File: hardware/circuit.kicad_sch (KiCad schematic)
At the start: 66 parts, among them J1 VBUS input fly-leads, J2 Shunt Kelvin, J3 Piezo fly-lead, J4 ESC1 signal, J5 ESC2 signal, J6 ELRS receiver, U1 Seeed XIAO RP2350, U10 SK9822-EC20, U2 AP63205WU-7, U3 MCP23S17T-E/SS, U4 H3LIS331DLTR, U5 H3LIS331DLTR, U6 H3LIS331DLTR, U7 INA180A1IDBVR, U8 SN74AHCT1G125, U9 SN74AHCT1G125

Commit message: feat: almost full schematic
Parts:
- removed C1, C4, C5: 22uF, Capacitor_SMD:C_0805_2012Metric, symbol Device:C_Small
- removed C12, C2, C3: 100nF, Capacitor_SMD:C_0402_1005Metric, symbol Device:C_Small
- removed C6: 10uF, Capacitor_SMD:C_0603_1608Metric, symbol Device:C_Small
- removed D1: BAT54S, Package_TO_SOT_SMD:SOT-23, symbol Diode:BAT54S
- removed J1: VBUS input fly-leads, Connector_Wire:SolderWire-0.5sqmm_1x02_P4.6mm_D0.9mm_OD2.1mm_Relief, symbol Connector_Generic:Conn_01x02
- removed J5: ESC2 signal, Connector_Wire:SolderWire-0.25sqmm_1x02_P4.2mm_D0.65mm_OD1.7mm_Relief, symbol Connector_Generic:Conn_01x02
- removed J6: ELRS receiver, Connector_Wire:SolderWire-0.25sqmm_1x04_P4.2mm_D0.65mm_OD1.7mm_Relief, symbol Connector_Generic:Conn_01x04
- removed L1: 4.7uH, Inductor_SMD:L_Wuerth_MAPI-4020, symbol Device:L_Small
- removed R10: 33kΩ, Resistor_SMD:R_0402_1005Metric, symbol Device:R_Small
- removed R9: 100kΩ, Resistor_SMD:R_0402_1005Metric, symbol Device:R_Small
- removed TP1: TP_SCK, TestPoint:TestPoint_Pad_D1.0mm, symbol Connector:TestPoint
- removed TP10: TP_VBAT, TestPoint:TestPoint_Pad_D1.0mm, symbol Connector:TestPoint
- removed TP12: TP_PIEZO, TestPoint:TestPoint_Pad_D1.0mm, symbol Connector:TestPoint
- removed TP16: TP_3V3, TestPoint:TestPoint_Pad_D1.0mm, symbol Connector:TestPoint
- removed TP17: TP_5V, TestPoint:TestPoint_Pad_D1.0mm, symbol Connector:TestPoint
- removed TP2: TP_CS_A, TestPoint:TestPoint_Pad_D1.0mm, symbol Connector:TestPoint
- removed TP3: TP_CS_B, TestPoint:TestPoint_Pad_D1.0mm, symbol Connector:TestPoint
- removed TP4: TP_CS_C, TestPoint:TestPoint_Pad_D1.0mm, symbol Connector:TestPoint
- removed TP5: TP_MISO, TestPoint:TestPoint_Pad_D1.0mm, symbol Connector:TestPoint
- removed TP6: TP_DS1, TestPoint:TestPoint_Pad_D1.0mm, symbol Connector:TestPoint
- removed TP7: TP_DS2, TestPoint:TestPoint_Pad_D1.0mm, symbol Connector:TestPoint
- removed TP8: TP_CRSF_RX, TestPoint:TestPoint_Pad_D1.0mm, symbol Connector:TestPoint
- removed TP9: TP_CRSF_TX, TestPoint:TestPoint_Pad_D1.0mm, symbol Connector:TestPoint
- removed U2: AP63205WU-7, Library:TSOT-23-6_L2.9-W1.6-P0.95-LS2.8-BL, symbol Library:AP63205WU-7
- removed U7: INA180A1IDBVR, Library:SOT-23-5_L3.0-W1.7-P0.95-LS2.8-BR, symbol Library:INA180A1IDBVR
- added C17, C21, C22: 22uF, Capacitor_SMD:C_0805_2012Metric, symbol Device:C_Small
- added C18, C20: 100nF, Capacitor_SMD:C_0402_1005Metric, symbol Device:C_Small
- added C19: 10uF, Capacitor_SMD:C_0603_1608Metric, symbol Device:C_Small
- added D3, D4: PESD5V0V1BB, Diode_SMD:D_SOD-523, symbol Device:D_TVS
- added D5: SMAJ12CA, Diode_SMD:D_SMA, symbol Device:D_TVS
- added L2: 4.7uH, Inductor_SMD:L_Wuerth_MAPI-4020, symbol Device:L_Small
- added Q1: AO3402, Library:SOT-23_L2.9-W1.3-P1.90-LS2.4-BR, symbol Library:AO3402_C14385
- added R16: 100Ω, Resistor_SMD:R_0402_1005Metric, symbol Device:R_Small
- added R17: 100kΩ, Resistor_SMD:R_0402_1005Metric, symbol Device:R_Small
- added R18: 33kΩ, Resistor_SMD:R_0402_1005Metric, symbol Device:R_Small
- added TP18: TP_3V3, TestPoint:TestPoint_Pad_D1.0mm, symbol Connector:TestPoint
- added TP19: TP_5V, TestPoint:TestPoint_Pad_D1.0mm, symbol Connector:TestPoint
- added U11: AP63205WU-7, Library:TSOT-23-6_L2.9-W1.6-P0.95-LS2.8-BL, symbol Library:AP63205WU-7
- added U7: BetaFPV ELRS Lite, Library:BetaFPV_ELRS_Lite, symbol Connector_Generic:Conn_01x04
- C13: value 10nF -> 100nF
- J2: value Shunt Kelvin -> Orange TinySLED
- J3: value Piezo fly-lead -> VBUS input fly-leads; footprint Connector_Wire:SolderWire-0.25sqmm_1x02_P4.2mm_D0.65mm_OD1.7mm_Relief -> Connector_Wire:SolderWire-0.5sqmm_1x02_P4.6mm_D0.9mm_OD2.1mm_Relief
- J4: value ESC1 signal -> AM32 dual ESC; footprint Connector_Wire:SolderWire-0.25sqmm_1x02_P4.2mm_D0.65mm_OD1.7mm_Relief -> Connector_Wire:SolderWire-0.25sqmm_1x04_P4.2mm_D0.65mm_OD1.7mm_Relief; symbol Connector_Generic:Conn_01x02 -> Connector_Generic:Conn_01x04
- R11: value 1MΩ -> 100kΩ
- TP11: value TP_CURR -> TP_VBAT
- U4: value H3LIS331DLTR -> LSM6DSV320XTR; footprint Library:LGA-16_L3.0-W3.0-P0.50-BL -> Library:LGA-14_L3.0-W2.5-P0.50-TL; symbol Library:H3LIS331DLTR -> Library:LSM6DSV320XTR; LCSC Part C2655074 -> C26633007
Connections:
- net 3V3: now also U4.5 (VDDIO), U4.8 (VDD), C19.1, TP18.1; no longer U4.1 (Vdd_IO), U4.14 (Vdd), U4.15 (Reserved)
- net 5V: now also C21.1, C22.1, L2.2, TP19.1, U11.1 (FB), U7.3 (Pin_3)
- net CRSF_RX: now also U7.2 (Pin_2)
- net CRSF_TX: now also U7.1 (Pin_1)
- net CS_A: now also U4.12 (CS); no longer U4.8 (CS)
- net GND: now also J4.1 (Pin_1), J4.4 (Pin_4), U4.2 (SDx), U4.3 (SCx), U4.6 (GND), U4.7 (GND), C17.2, C18.2, C19.2, C21.2, C22.2, D3.2 (A2), D4.2 (A2), D5.2 (A2), Q1.2 (S), R17.2, R18.2, U11.4 (GND), U7.4 (Pin_4); no longer J4.2 (Pin_2), R11.2, U4.10 (Reserved), U4.12 (GND), U4.13 (GND), U4.16 (GND), U4.5 (GND)
- net LED_OE_N: now also U1.3 (D2/A2/GPIO42); no longer U3.24 (GPA3)
- net MISO_A: now also U4.1 (SDO/TA0); no longer U4.7 (SDO/SA0)
- net SPI_MOSI: now also U4.14 (SDA); no longer U4.6 (SDA/SDI/SDO)
- net SPI_SCK: now also U4.13 (SCL); no longer U4.4 (SCL/SPS)
- net VBAT_SNS: now also C13.1, R11.2, TP11.1, R18.1
- net VBUS: now also J2.1 (Pin_1), J3.1 (Pin_1), R11.1, C17.1, C18.1, D5.1 (A1), U11.2 (EN), U11.3 (VIN)
- net at R12.2: now also J4.2 (Pin_2), D3.1 (A1); no longer J4.1 (Pin_1)
- net at R13.2: now also J4.3 (Pin_3), D4.1 (A1)
- net CURR_SNS renamed HEAD_LED
- net HEAD_LED: now also R16.1; no longer TP11.1
- removed net PIEZO: C13.1, J3.1 (Pin_1), R11.1, U1.3 (D2/A2/GPIO42)
- net SHUNT_N: no longer names the net of J2.2 (Pin_2)
- net SHUNT_N: now also Q1.3 (D)
- new net: C20.1, U11.6 (BST)
- new net: C20.2, L2.1, U11.5 (SW)
- new net: Q1.1 (G), R16.2, R17.1
- no-connect marks 39 -> 40
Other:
- added sheet Power Subsystem (schm/power.kicad_sch)
- note added: "Tiny SLED"
- note removed: "Current sense"
- note removed: "Piezo impact input"
- company: (none) -> Dunkirk Corp
- title: (none) -> Holy Guacamole
- moved on the sheet: C10, C14, C15, C16, C7, C8, C9, J2, R1, R12, R14, R15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

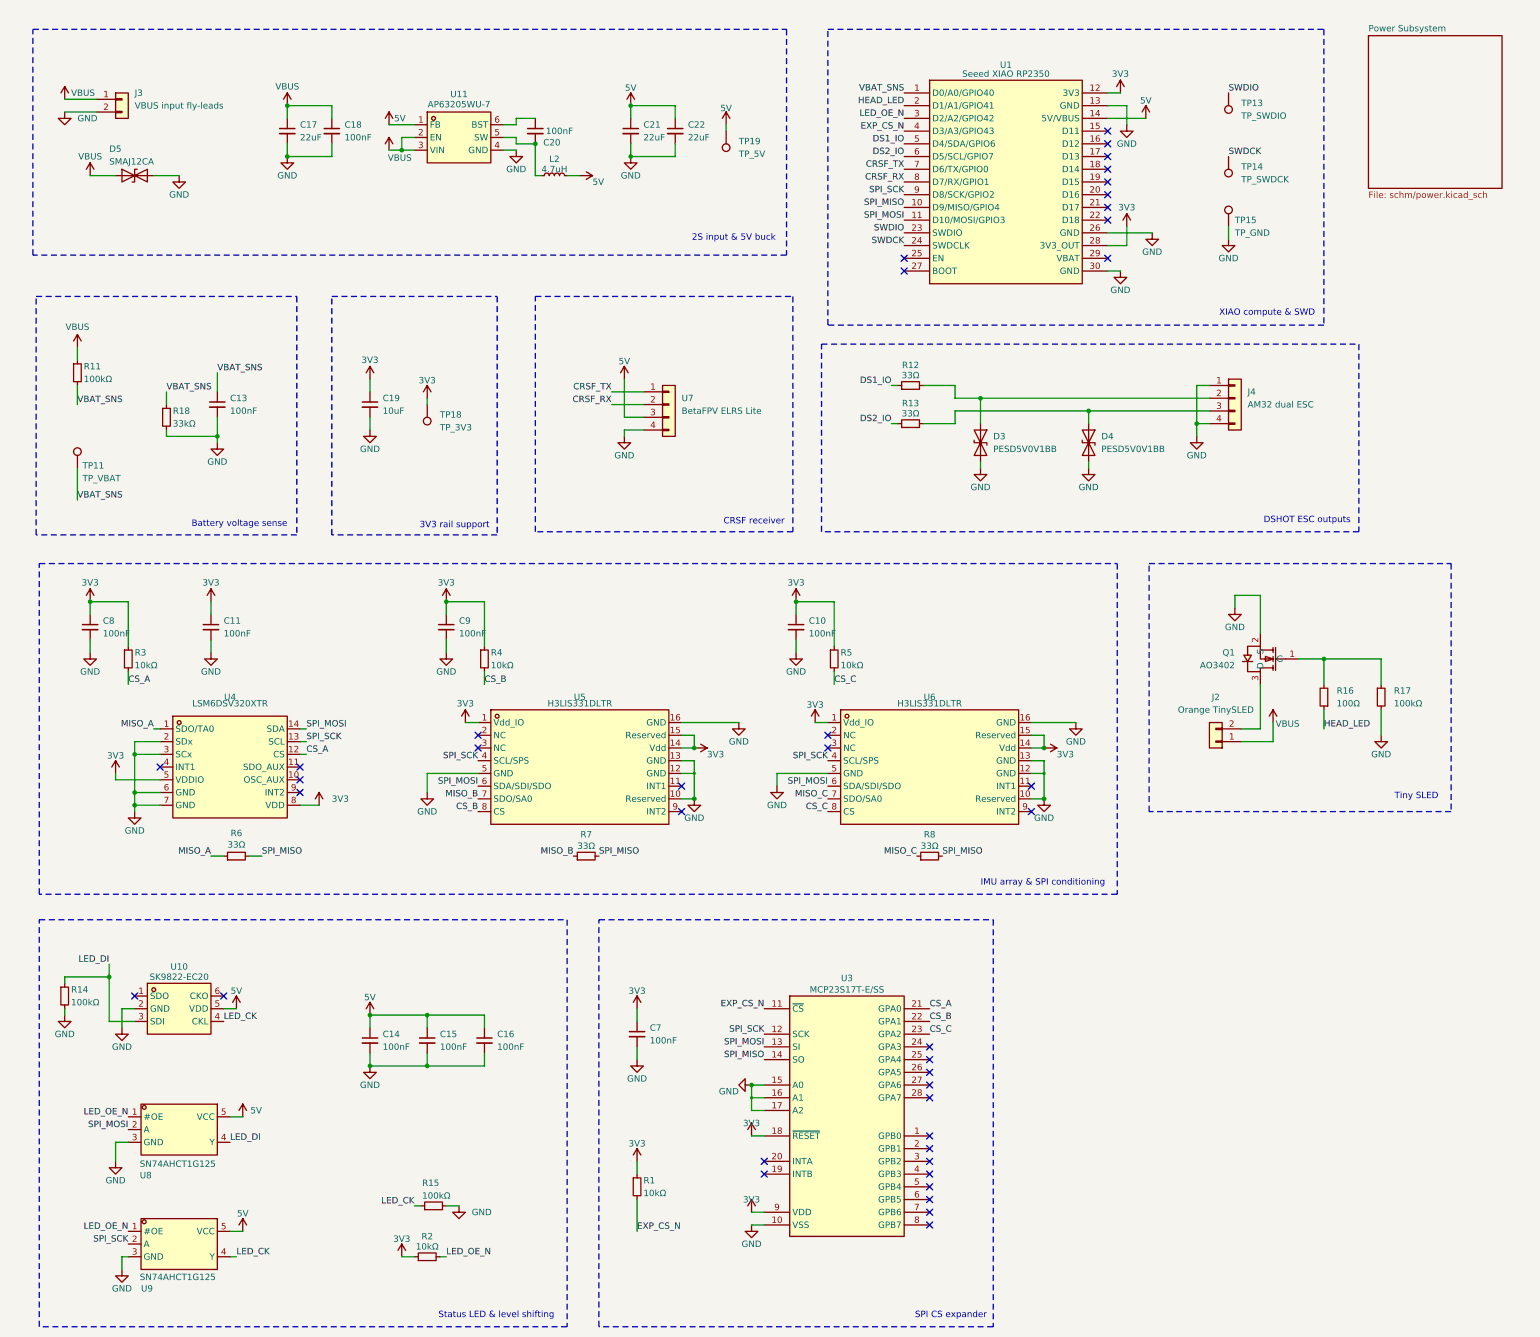
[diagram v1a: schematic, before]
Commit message: feat: organize into hierarchical sheets
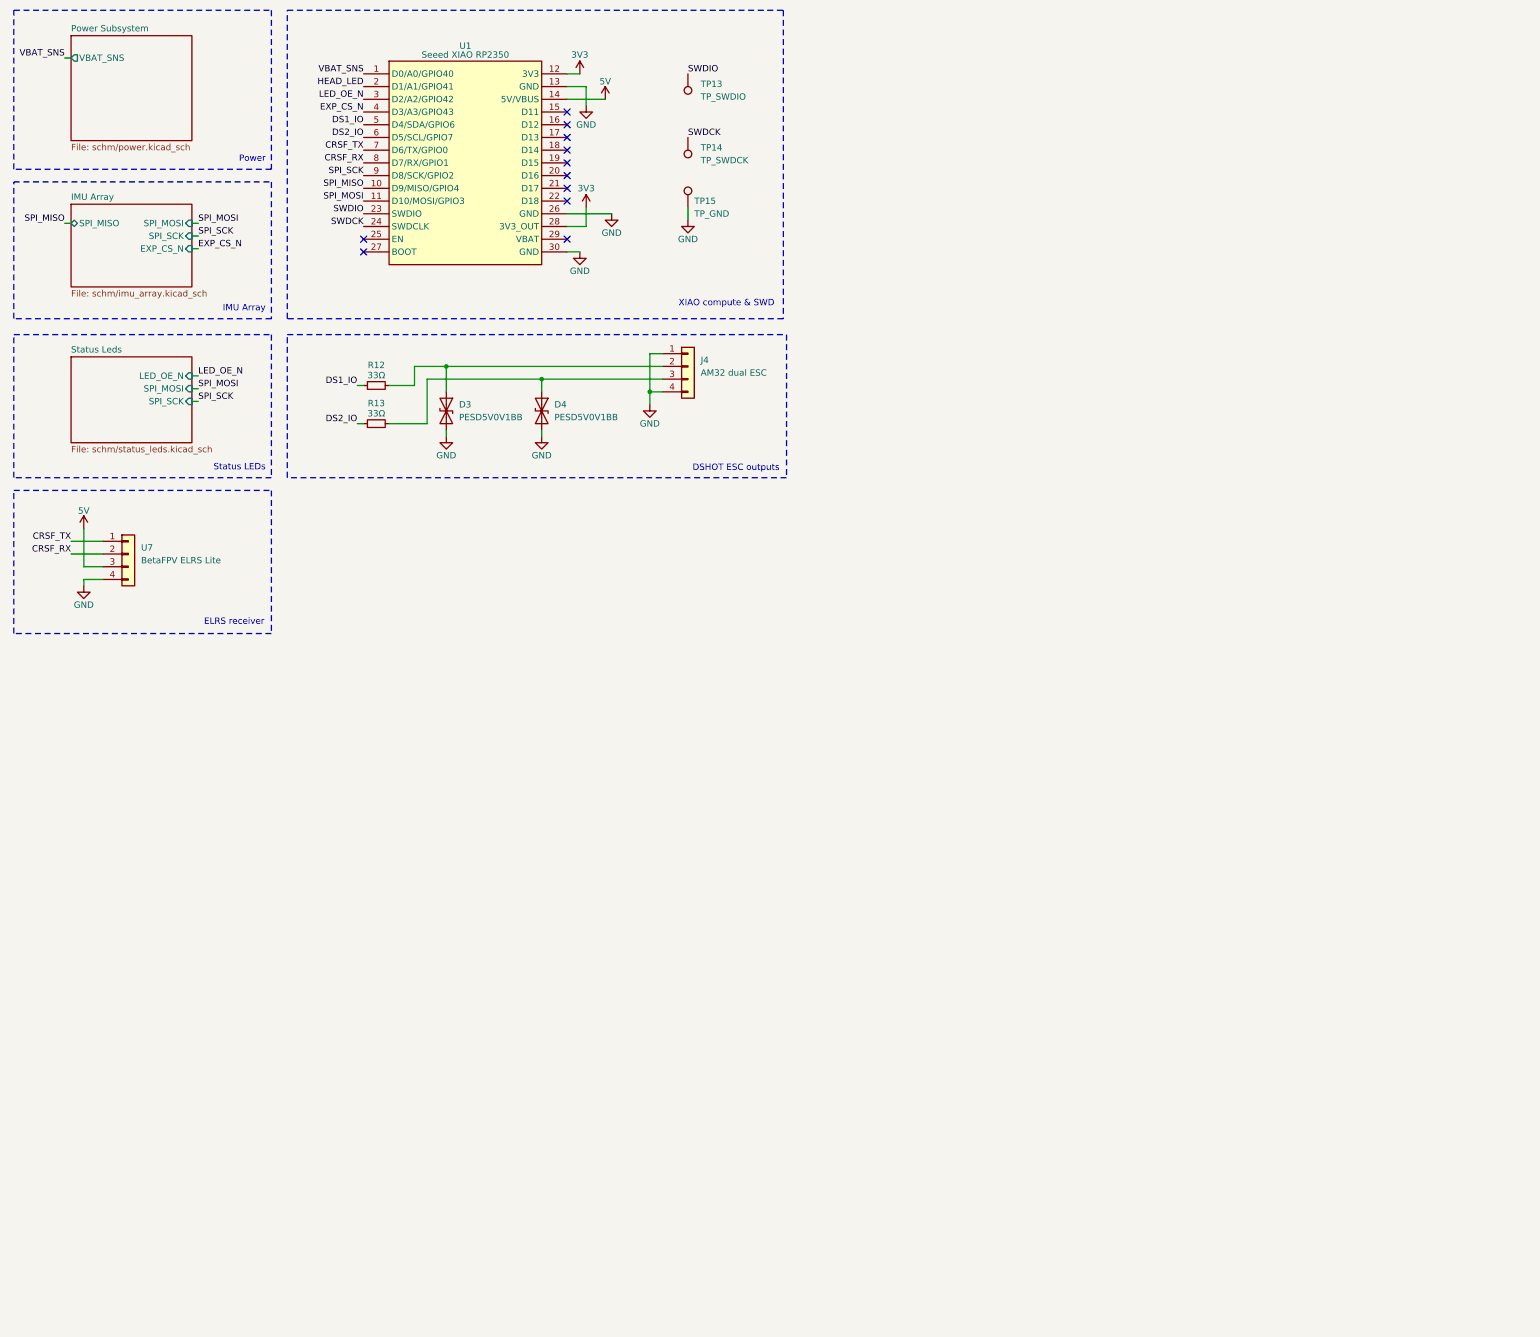
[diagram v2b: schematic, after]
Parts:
- removed C10, C11, C13, C14, C15, C16, C18, C20, C7, C8, C9: 100nF, Capacitor_SMD:C_0402_1005Metric, symbol Device:C_Small
- removed C17, C21, C22: 22uF, Capacitor_SMD:C_0805_2012Metric, symbol Device:C_Small
- removed C19: 10uF, Capacitor_SMD:C_0603_1608Metric, symbol Device:C_Small
- removed D5: SMAJ12CA, Diode_SMD:D_SMA, symbol Device:D_TVS
- removed J2: Orange TinySLED, Connector_Wire:SolderWire-0.25sqmm_1x02_P4.2mm_D0.65mm_OD1.7mm_Relief, symbol Connector_Generic:Conn_01x02
- removed J3: VBUS input fly-leads, Connector_Wire:SolderWire-0.5sqmm_1x02_P4.6mm_D0.9mm_OD2.1mm_Relief, symbol Connector_Generic:Conn_01x02
- removed L2: 4.7uH, Inductor_SMD:L_Wuerth_MAPI-4020, symbol Device:L_Small
- removed Q1: AO3402, Library:SOT-23_L2.9-W1.3-P1.90-LS2.4-BR, symbol Library:AO3402_C14385
- removed R1, R2, R3, R4, R5: 10kΩ, Resistor_SMD:R_0402_1005Metric, symbol Device:R_Small
- removed R11, R14, R15, R17: 100kΩ, Resistor_SMD:R_0402_1005Metric, symbol Device:R_Small
- removed R16: 100Ω, Resistor_SMD:R_0402_1005Metric, symbol Device:R_Small
- removed R18: 33kΩ, Resistor_SMD:R_0402_1005Metric, symbol Device:R_Small
- removed R6, R7, R8: 33Ω, Resistor_SMD:R_0402_1005Metric, symbol Device:R_Small
- removed TP11: TP_VBAT, TestPoint:TestPoint_Pad_D1.0mm, symbol Connector:TestPoint
- removed TP18: TP_3V3, TestPoint:TestPoint_Pad_D1.0mm, symbol Connector:TestPoint
- removed TP19: TP_5V, TestPoint:TestPoint_Pad_D1.0mm, symbol Connector:TestPoint
- removed U10: SK9822-EC20, Library:LED-SMD_6P-L2.0-W2.0-P0.80-TL, symbol Library:SK9822-EC20
- removed U11: AP63205WU-7, Library:TSOT-23-6_L2.9-W1.6-P0.95-LS2.8-BL, symbol Library:AP63205WU-7
- removed U3: MCP23S17T-E/SS, Library:SSOP-28_L10.2-W5.3-P0.65-LS7.8-BL, symbol Library:MCP23S17T-E_SS
- removed U4: LSM6DSV320XTR, Library:LGA-14_L3.0-W2.5-P0.50-TL, symbol Library:LSM6DSV320XTR
- removed U5, U6: H3LIS331DLTR, Library:LGA-16_L3.0-W3.0-P0.50-BL, symbol Library:H3LIS331DLTR
- removed U8, U9: SN74AHCT1G125, Library:SC-70-5_L2.0-W1.3-P0.65-LS2.1-BL, symbol Library:SN74AHCT1G125DCKR
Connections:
- no-connect marks 40 -> 11
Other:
- added sheet IMU Array (schm/imu_array.kicad_sch)
- added sheet Status Leds (schm/status_leds.kicad_sch)
- sheet Power Subsystem ports: added VBAT_SNS; removed none
- note added: "ELRS receiver"
- note added: "IMU Array"
- note added: "Power"
- note added: "Status LEDs"
- note removed: "2S input & 5V buck"
- note removed: "3V3 rail support"
- note removed: "Battery voltage sense"
- note removed: "CRSF receiver"
- note removed: "IMU array & SPI conditioning"
- note removed: "SPI CS expander"
- note removed: "Status LED & level shifting"
- note removed: "Tiny SLED"
- company: Dunkirk Corp -> Kieran Klukas
- moved on the sheet: D3, D4, J4, R12, R13, TP13, TP14, TP15, U1, U7
